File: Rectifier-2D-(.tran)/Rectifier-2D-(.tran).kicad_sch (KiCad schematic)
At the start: 6 parts

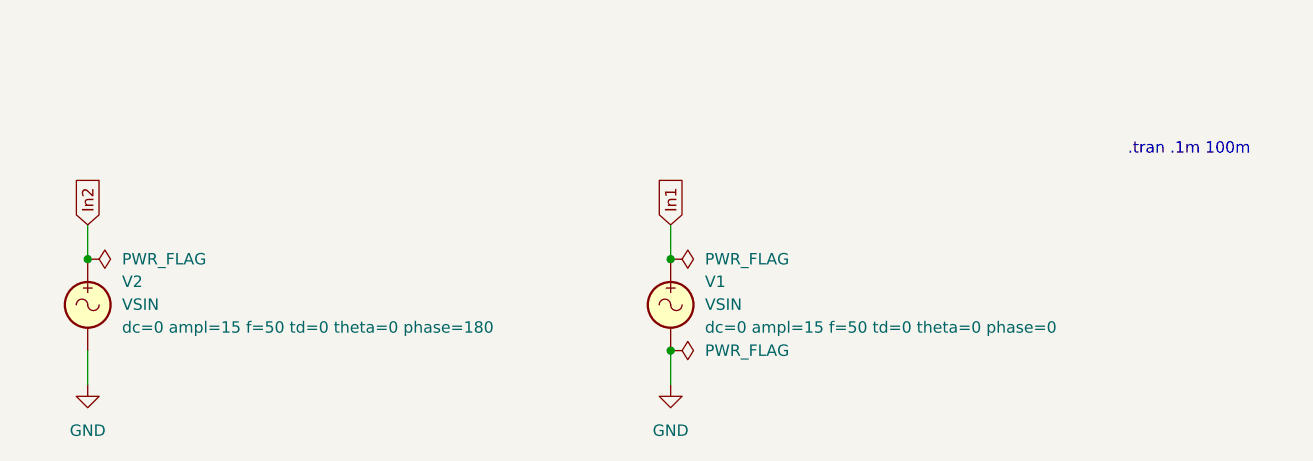
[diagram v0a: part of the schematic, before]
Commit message: Updated all schematics and prepared for KiCad 8.0
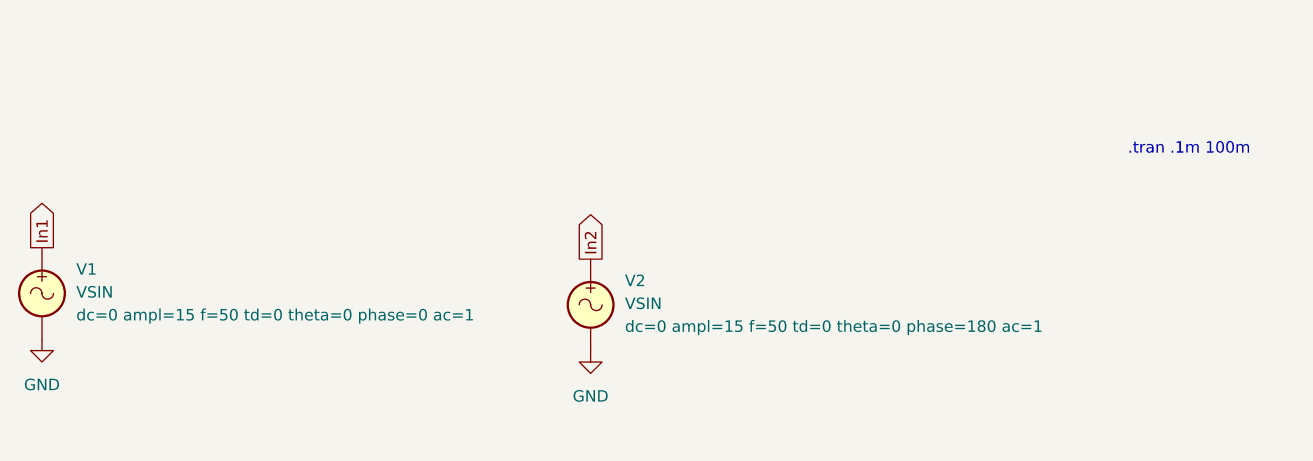
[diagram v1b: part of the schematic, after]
